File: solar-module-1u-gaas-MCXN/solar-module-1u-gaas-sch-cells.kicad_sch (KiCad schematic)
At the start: 3 parts

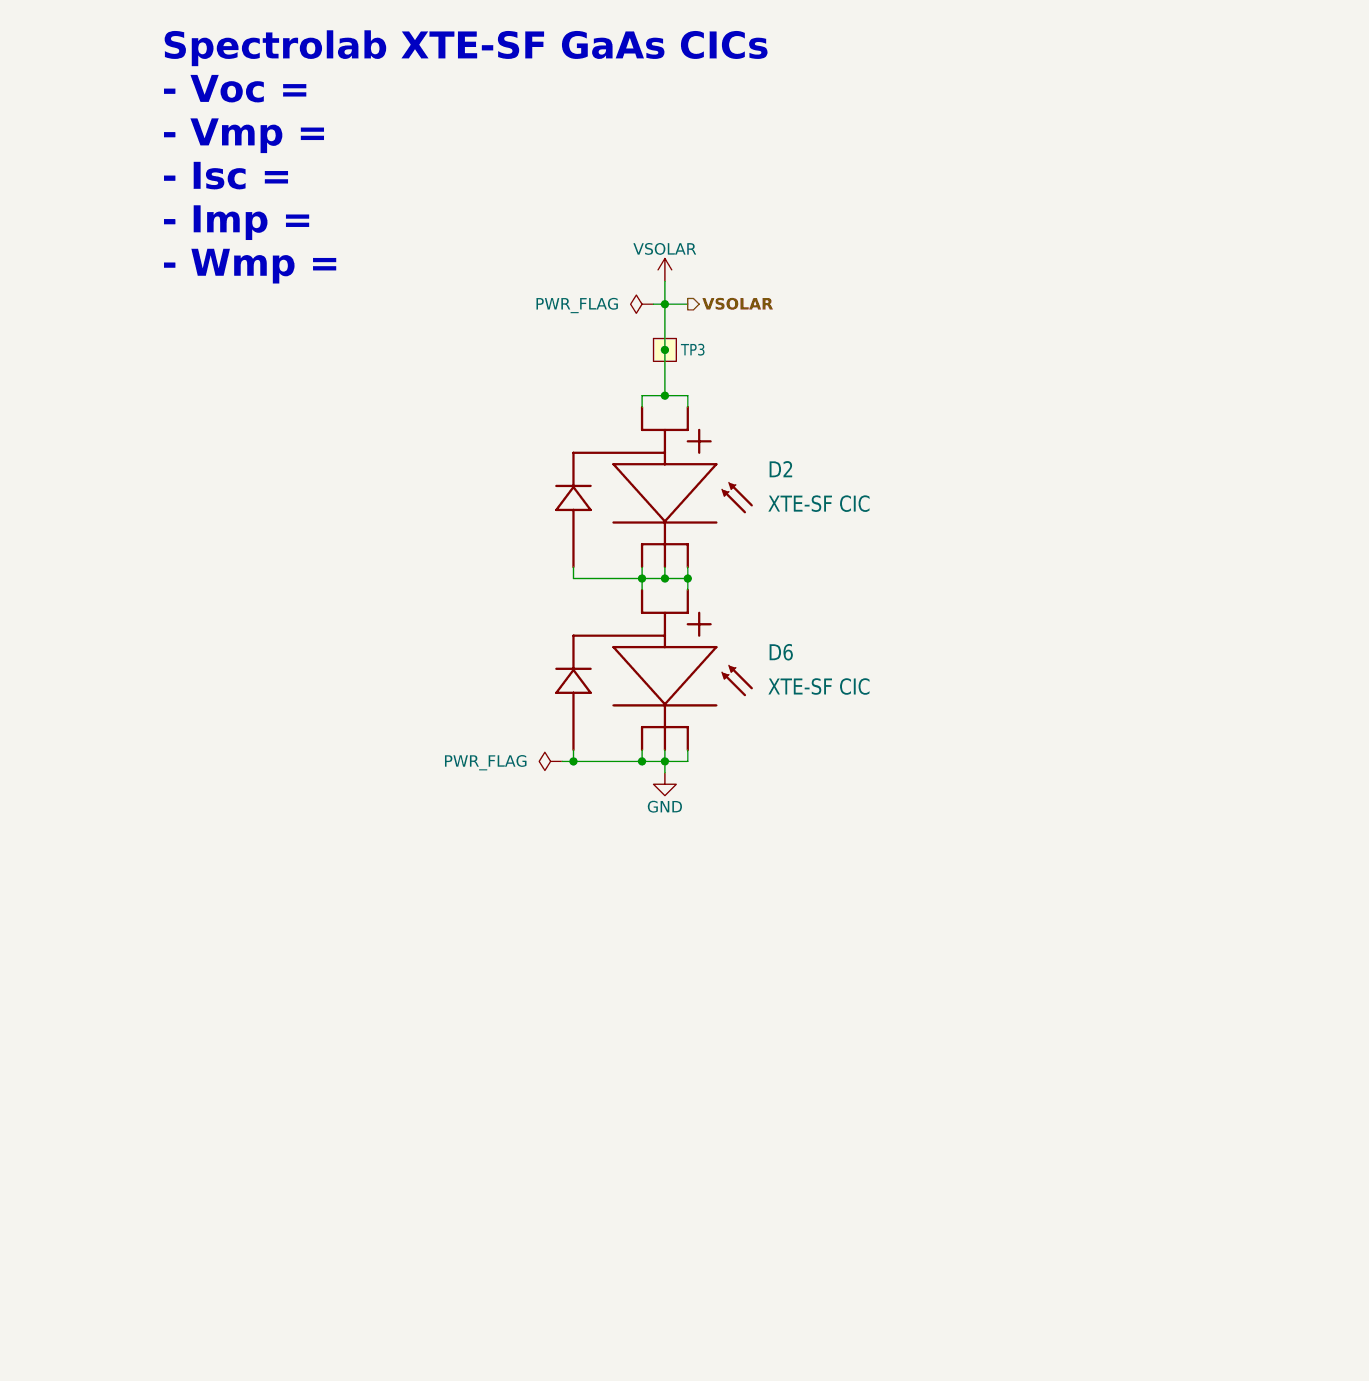
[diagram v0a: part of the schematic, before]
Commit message: Solar Module with GaAs Cells and MCXN processor v1.1
Fixed BOM, fixed solar connector sync between brd/sch, routed UART lines to the connector, untented vias for venting. Sent to fab.
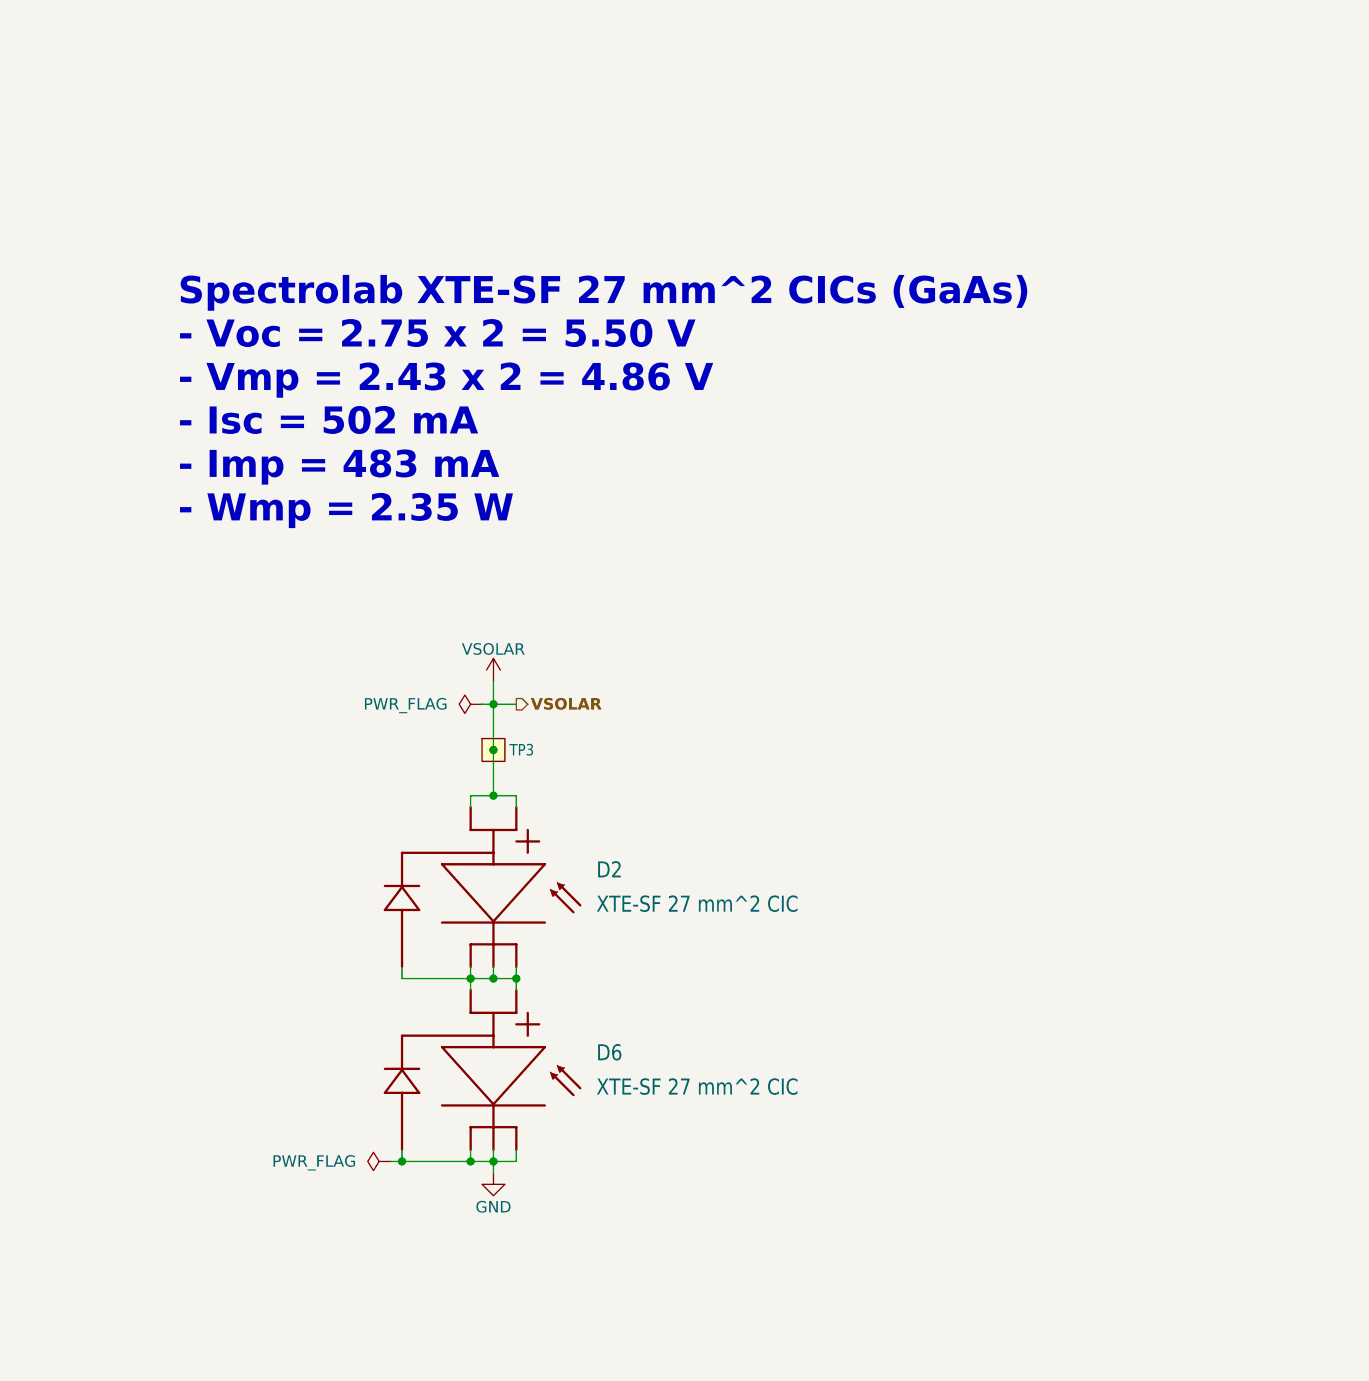
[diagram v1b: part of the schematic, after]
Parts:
- D2, D6: value XTE-SF CIC -> XTE-SF 27 mm^2 CIC; DIS (none) -> N/A; DPN (none) -> N/A; MFR (none) -> SpectraLabs; MPN (none) -> XTE-SF 27 mm^2 CIC
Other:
- note added: "Spectrolab XTE-SF 27 mm^2 CICs (GaAs) - Voc = 2.75 x 2 = 5.50 V - Vmp = 2.43 x 2 = 4.86 V - Isc = 502 mA - Imp = 483 mA - Wmp = 2.35 W"
- note removed: "Spectrolab XTE-SF GaAs CICs - Voc = - Vmp = - Isc = - Imp = - Wmp ="
- moved on the sheet: D2, D6, TP3
